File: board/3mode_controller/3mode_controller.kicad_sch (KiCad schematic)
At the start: 41 parts, among them IC1 DW01A, J1 Conn_01x04_Socket, J2 USB_C_Receptacle, Q1 FDN336P, SW1 reset, SW2 ChangeScreen, SW2 boot, SW4 SW_SPDT, U1 TP4056, U2 ESP32-S3-WROOM-1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

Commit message: first pcb version
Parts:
- removed R17 (x2): 5.1K, Resistor_SMD:R_0603_1608Metric_Pad0.98x0.95mm_HandSolder, symbol Device:R
- added H1, H2: MountingHole, MountingHole:MountingHole_3.2mm_M3_ISO14580_Pad, symbol Mechanical:MountingHole
- J1: footprint (none) -> Connector_PinHeader_2.54mm:PinHeader_1x04_P2.54mm_Vertical
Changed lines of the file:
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@@
   (junction (at 49.53 211.455) (diameter 0) (color 0 0 0 0)
   )
-  (junction (at 327.66 34.29) (diameter 0) (color 0 0 0 0)
-  )
   (junction (at 39.37 197.485) (diameter 0) (color 0 0 0 0)
   )
@@
   (junction (at 118.745 153.67) (diameter 0) (color 0 0 0 0)
   )
-  (junction (at 330.2 43.815) (diameter 0) (color 0 0 0 0)
-  )
   (junction (at 238.125 42.545) (diameter 0) (color 0 0 0 0)
   )
   (junction (at 41.275 45.085) (diameter 0) (color 0 0 0 0)
   )
-  (junction (at 325.12 54.61) (diameter 0) (color 0 0 0 0)
-  )
   (junction (at 215.265 56.515) (diameter 0) (color 0 0 0 0)
   )
@@
   )
   (junction (at 84.455 143.51) (diameter 0) (color 0 0 0 0)
-  )
-  (junction (at 325.12 45.72) (diameter 0) (color 0 0 0 0)
   )
   (junction (at 215.265 61.595) (diameter 0) (color 0 0 0 0)
@@
     (stroke (width 0) (type default))
   )
-  (wire (pts (xy 327.66 34.29) (xy 327.66 35.56))
-    (stroke (width 0) (type default))
-  )
   (wire (pts (xy 47.625 170.18) (xy 47.625 171.45))
     (stroke (width 0) (type default))
@@
     (stroke (width 0) (type default))
   )
-  (wire (pts (xy 330.2 52.705) (xy 330.2 54.61))
-    (stroke (width 0) (type default))
-  )
   (wire (pts (xy 39.37 233.045) (xy 49.53 233.045))
     (stroke (width 0) (type default))
@@
     (stroke (width 0) (type default))
   )
-  (wire (pts (xy 327.66 43.18) (xy 327.66 45.72))
-    (stroke (width 0) (type default))
-  )
   (wire (pts (xy 82.55 211.455) (xy 83.82 211.455))
     (stroke (width 0) (type default))
   )
-  (wire (pts (xy 327.66 45.72) (xy 325.12 45.72))
-    (stroke (width 0) (type default))
-  )
   (wire (pts (xy 327.66 33.655) (xy 327.66 34.29))
     (stroke (width 0) (type default))
@@
     (stroke (width 0) (type default))
   )
-  (wire (pts (xy 330.2 43.815) (xy 330.2 45.085))
-    (stroke (width 0) (type default))
-  )
   (wire (pts (xy 39.37 194.945) (xy 39.37 197.485))
     (stroke (width 0) (type default))
@@
     (stroke (width 0) (type default))
   )
-  (wire (pts (xy 325.12 33.655) (xy 325.12 45.72))
-    (stroke (width 0) (type default))
-  )
   (wire (pts (xy 215.265 61.595) (xy 215.265 62.865))
     (stroke (width 0) (type default))
@@
     (stroke (width 0) (type default))
   )
-  (wire (pts (xy 325.12 45.72) (xy 325.12 54.61))
-    (stroke (width 0) (type default))
-  )
   (wire (pts (xy 47.625 161.29) (xy 48.895 161.29))
     (stroke (width 0) (type default))
@@
     (stroke (width 0) (type default))
   )
-  (wire (pts (xy 325.12 54.61) (xy 325.12 55.245))
+  (wire (pts (xy 325.12 33.655) (xy 325.12 55.245))
     (stroke (width 0) (type default))
   )
@@
   )
   (wire (pts (xy 329.565 106.045) (xy 332.105 106.045))
-    (stroke (width 0) (type default))
-  )
-  (wire (pts (xy 330.2 54.61) (xy 325.12 54.61))
     (stroke (width 0) (type default))
   )
@@
     )
   )
+  (symbol (lib_id "Mechanical:MountingHole") (at 354.965 117.475 0) (unit 1)
+    (in_bom yes) (on_board yes) (dnp no)
+    (property "Reference" "H1" (at 358.14 116.2081 0)
+      (effects (font (size 1.27 1.27)) (justify left))
+    )
+    (property "Value" "MountingHole" (at 358.14 118.745 0)
+      (effects (font (size 1.27 1.27)) (justify left))
+    )
+    (property "Footprint" "MountingHole:MountingHole_3.2mm_M3_ISO14580_Pad" (at 354.965 117.475 0)
+      (effects (font (size 1.27 1.27)) hide)
+    )
+    (property "Datasheet" "~" (at 354.965 117.475 0)
+      (effects (font (size 1.27 1.27)) hide)
+    )
+    (instances
+      (project "bubblebutbot"
+        (path "/2cd1342d-9ef7-44f7-8a7d-ec49b5dc5750"
+          (reference "H1") (unit 1)
+        )
+      )
+      (project "3mode_controller"
+        (path "/64deb2d4-0f1e-4037-b447-7d4c34ae11e6"
+          (reference "H3") (unit 1)
+        )
+      )
+    )
+  )
   (symbol (lib_id "power:GND") (at 225.425 172.085 0) (unit 1)
     (in_bom yes) (on_board yes) (dnp no) (fields_autoplaced)
@@
       (effects (font (size 1.27 1.27)))
     )
-    (property "Footprint" "" (at 325.12 28.575 0)
+    (property "Footprint" "Connector_PinHeader_2.54mm:PinHeader_1x04_P2.54mm_Vertical" (at 325.12 28.575 0)
       (effects (font (size 1.27 1.27)) hide)
     )
@@
     )
   )
-  (symbol (lib_id "Device:R") (at 330.2 48.895 180) (unit 1)
-    (in_bom yes) (on_board yes) (dnp no)
-    (property "Reference" "R17" (at 331.978 47.6829 0)
-      (effects (font (size 1.27 1.27)) (justify right))
-    )
-    (property "Value" "5.1K" (at 331.978 50.1071 0)
-      (effects (font (size 1.27 1.27)) (justify right))
-    )
-    (property "Footprint" "Resistor_SMD:R_0603_1608Metric_Pad0.98x0.95mm_HandSolder" (at 331.978 48.895 90)
-      (effects (font (size 1.27 1.27)) hide)
-    )
-    (property "Datasheet" "https://www.lcsc.com/product-detail/Chip-Resistor-Surface-Mount_FOJAN-FRC0603J512-TS_C2907114.html" (at 330.2 48.895 0)
-      (effects (font (size 1.27 1.27)) hide)
-    )
-    (property "LCSC" "C2907114" (at 330.2 48.895 90)
-      (effects (font (size 1.27 1.27)) hide)
-    )
-    (pin "1")
-    (pin "2")
-    (instances
-      (project "bubblebutbot"
-        (path "/2cd1342d-9ef7-44f7-8a7d-ec49b5dc5750"
-          (reference "R17") (unit 1)
-        )
-      )
-      (project "3mode_controller"
-        (path "/64deb2d4-0f1e-4037-b447-7d4c34ae11e6"
-          (reference "R11") (unit 1)
-        )
-      )
-    )
-  )
   (symbol (lib_id "power:+5V") (at 238.125 42.545 0) (unit 1)
     (in_bom yes) (on_board yes) (dnp no) (fields_autoplaced)
@@
     )
   )
-  (symbol (lib_id "Device:R") (at 327.66 39.37 180) (unit 1)
-    (in_bom yes) (on_board yes) (dnp no)
-    (property "Reference" "R17" (at 330.835 38.2158 0)
-      (effects (font (size 1.27 1.27)) (justify right))
-    )
-    (property "Value" "5.1K" (at 330.835 40.64 0)
-      (effects (font (size 1.27 1.27)) (justify right))
-    )
-    (property "Footprint" "Resistor_SMD:R_0603_1608Metric_Pad0.98x0.95mm_HandSolder" (at 329.438 39.37 90)
-      (effects (font (size 1.27 1.27)) hide)
-    )
-    (property "Datasheet" "https://www.lcsc.com/product-detail/Chip-Resistor-Surface-Mount_FOJAN-FRC0603J512-TS_C2907114.html" (at 327.66 39.37 0)
-      (effects (font (size 1.27 1.27)) hide)
-    )
-    (property "LCSC" "C2907114" (at 327.66 39.37 90)
-      (effects (font (size 1.27 1.27)) hide)
-    )
-    (pin "1")
-    (pin "2")
-    (instances
-      (project "bubblebutbot"
-        (path "/2cd1342d-9ef7-44f7-8a7d-ec49b5dc5750"
-          (reference "R17") (unit 1)
-        )
-      )
-      (project "3mode_controller"
-        (path "/64deb2d4-0f1e-4037-b447-7d4c34ae11e6"
-          (reference "R8") (unit 1)
-        )
-      )
-    )
-  )
   (symbol (lib_id "power:GND") (at 80.645 170.18 0) (unit 1)
     (in_bom yes) (on_board yes) (dnp no) (fields_autoplaced)
@@
         )
       )
+    )
+  )
+  (symbol (lib_id "Mechanical:MountingHole") (at 354.965 123.19 0) (unit 1)
+    (in_bom yes) (on_board yes) (dnp no)
+    (property "Reference" "H2" (at 358.14 121.9231 0)
+      (effects (font (size 1.27 1.27)) (justify left))
+    )
+    (property "Value" "MountingHole" (at 358.14 124.46 0)
+      (effects (font (size 1.27 1.27)) (justify left))
+    )
+    (property "Footprint" "MountingHole:MountingHole_3.2mm_M3_ISO14580_Pad" (at 354.965 123.19 0)
+      (effects (font (size 1.27 1.27)) hide)
+    )
+    (property "Datasheet" "~" (at 354.965 123.19 0)
+      (effects (font (size 1.27 1.27)) hide)
+    )
+    (instances
+      (project "bubblebutbot"
+        (path "/2cd1342d-9ef7-44f7-8a7d-ec49b5dc5750"
+          (reference "H2") (unit 1)
+        )
+      )
+      (project "3mode_controller"
+        (path "/64deb2d4-0f1e-4037-b447-7d4c34ae11e6"
+          (reference "H4") (unit 1)
+        )
+      )

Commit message: updated one missing footprint
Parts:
- Q1: LCSC C475693 -> C19188376
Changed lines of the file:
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@@
       (effects (font (size 1.27 1.27) italic) (justify left) hide)
     )
-    (property "Datasheet" "https://datasheet.lcsc.com/lcsc/2001131004_Shikues-FDN336P_C475693.pdf" (at 111.125 151.13 0)
+    (property "Datasheet" "https://www.lcsc.com/product-detail/MOSFETs_Slkor-SLKORMICRO-Elec-FDN336P_C19188376.html" (at 111.125 151.13 0)
       (effects (font (size 1.27 1.27)) (justify left) hide)
     )
-    (property "LCSC" "C475693" (at 111.125 151.13 0)
+    (property "LCSC" "C19188376" (at 111.125 151.13 0)
       (effects (font (size 1.27 1.27)) hide)
     )

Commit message: first prototype board
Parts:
- removed C2: 10u, Capacitor_SMD:C_0603_1608Metric_Pad1.08x0.95mm_HandSolder, symbol Device:C
- removed H1, H2: MountingHole, MountingHole:MountingHole_3.2mm_M3_ISO14580_Pad, symbol Mechanical:MountingHole
- removed J1: Conn_01x04_Socket, Connector_PinHeader_2.54mm:PinHeader_1x04_P2.54mm_Vertical, symbol Connector:Conn_01x04_Socket
- removed SW2: ChangeScreen, Button_Switch_THT:SW_PUSH_6mm, symbol Switch:SW_Push
- removed U3: 18350-HOLDER, CustomFootprints:18350-Holder, symbol CustomSymbols:18350-HOLDER
- added J1: JST XH, Connector_JST:JST_PH_S2B-PH-K_1x02_P2.00mm_Horizontal, symbol Connector:Conn_01x02_Socket
- added SW3: SW_DIP_x04, Button_Switch_THT:SW_DIP_SPSTx04_Slide_9.78x12.34mm_W7.62mm_P2.54mm, symbol Switch:SW_DIP_x04
- U7, U8: LCSC C146170 -> C918854
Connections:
- net GND: now also U7.7 (SWa), U8.7 (SWa), SW3.5, SW3.6, SW3.7, SW3.8; no longer U7.9 (SWc), U8.9 (SWc)
- net VBAT+PROTECT: now also J1.1 (Pin_1)
- net JS_LEFT_IRQ: now reaches U7.8 (SWb)
- net JS_LEFT_IRQ: now also U2.22 (GPIO14/TOUCH14/ADC2_CH3/FSPIWP/FSPIDQS/SUBSPIWP)
- net at C4.2, IC1.6 (GND), U4.1 (S1): now also J1.2 (Pin_2)
- net JS_RIGHT_IRQ: now reaches U2.10 (GPIO17/U1TXD/ADC2_CH6)
- net JS_RIGHT_IRQ: now also U8.8 (SWb)
- net ESP32-PULLUP-1: now reaches U2.6 (GPIO6/TOUCH6/ADC1_CH5)
- net ESP32-PULLUP-1: now also SW3.4
- net ESP32-PULLUP-2: now reaches U2.7 (GPIO7/TOUCH7/ADC1_CH6)
- net ESP32-PULLUP-2: now also SW3.3
- net ESP32_BUTTON: no longer names the net of U2.5 (GPIO5/TOUCH5/ADC1_CH4)
- net ESP32_SCREEN_SCK renamed ESP32-PULLUP-3
- net ESP32-PULLUP-3: now also SW3.2
- net ESP32_SCREEN_SDA renamed ESP32-PULLUP-4
- net ESP32-PULLUP-4: now also SW3.1
- no-connect marks 47 -> 42
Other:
- note added: "Joystick RKJXV122400R Lever returns to center."
- note added: "swB = interrupt swA = grounded"
- note removed: "swd = interrupt swc = grounded"
- moved on the sheet: C13, R1, U2, U7, U8

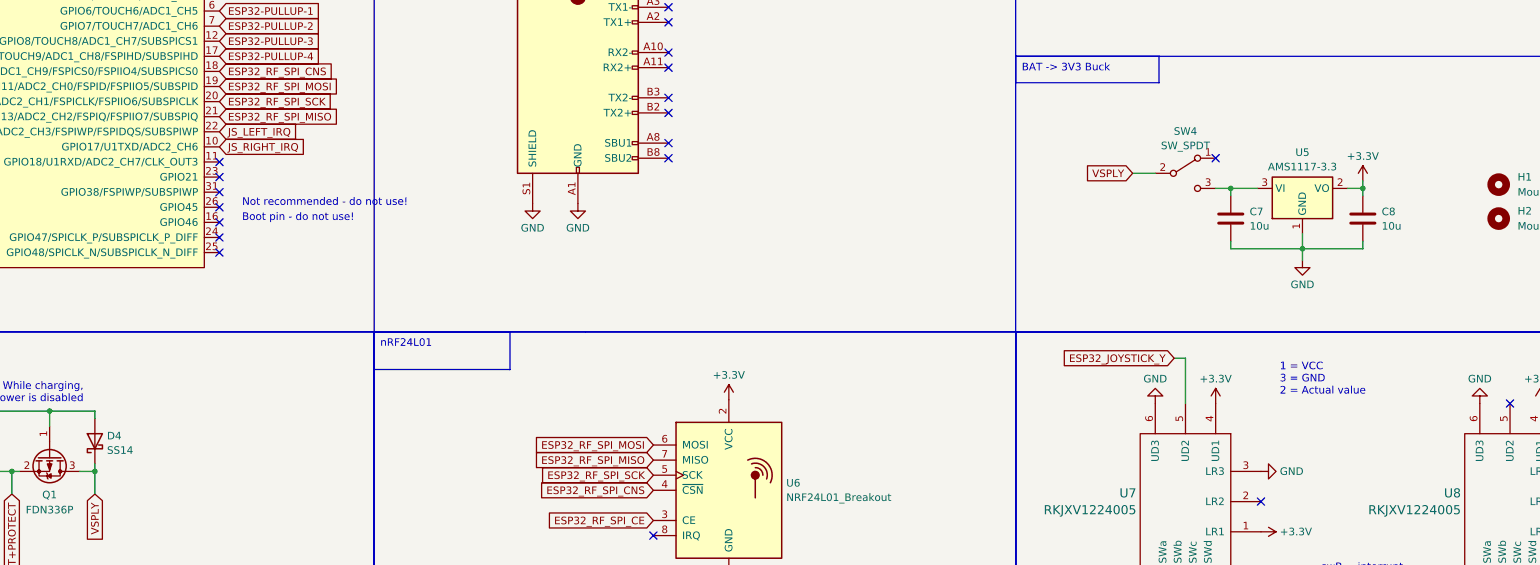
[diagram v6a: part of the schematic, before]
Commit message: v0.2.
Replaced diode and LDO
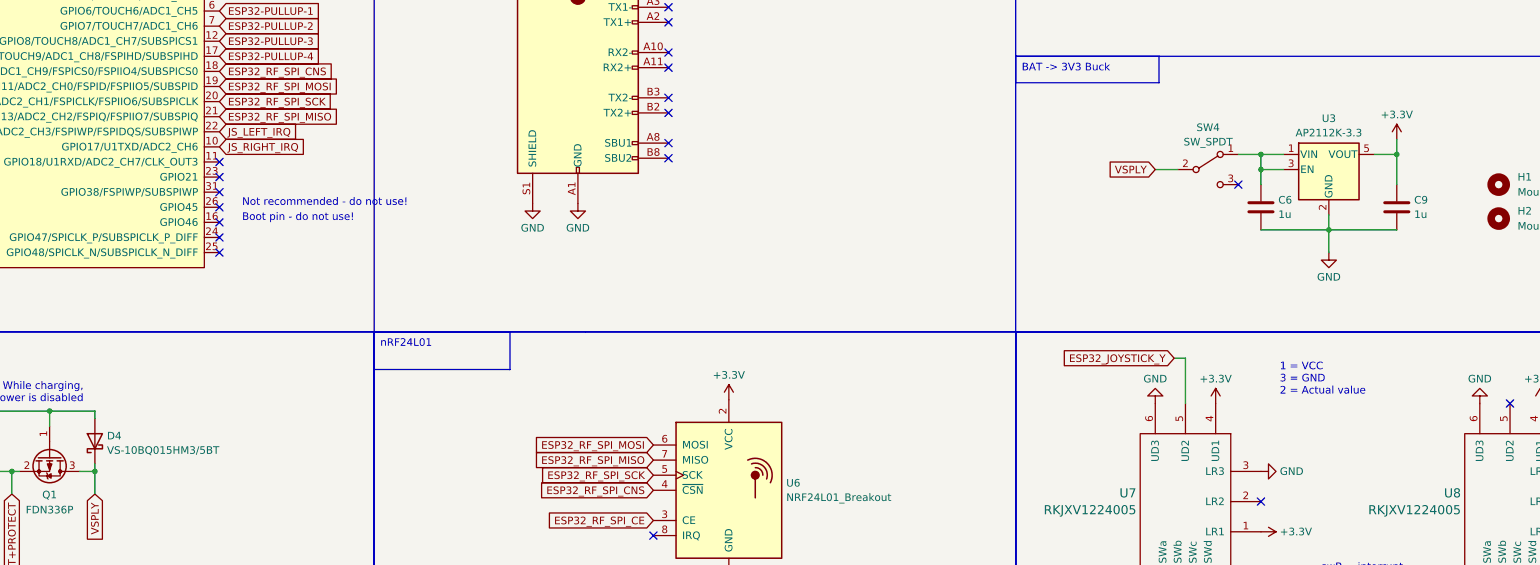
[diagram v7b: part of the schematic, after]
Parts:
- removed C7, C8: 10u, Capacitor_Tantalum_SMD:CP_EIA-3216-18_Kemet-A_Pad1.58x1.35mm_HandSolder, symbol Device:C
- removed U5: AMS1117-3.3, Package_TO_SOT_SMD:SOT-223-3_TabPin2, symbol Regulator_Linear:AMS1117-3.3
- added C6, C9: 1u, Capacitor_SMD:C_0603_1608Metric_Pad1.08x0.95mm_HandSolder, symbol Device:C
- added U3: AP2112K-3.3, Package_TO_SOT_SMD:SOT-23-5, symbol Regulator_Linear:AP2112K-3.3
- D4: value SS14 -> VS-10BQ015HM3/5BT; footprint Diode_SMD:D_SMA -> Diode_SMD:D_SMB; LCSC C2480 -> C413465
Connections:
- net +3.3V: now also C9.1, U3.5 (VOUT)
- net GND: now also C6.2, C9.2, U3.2 (GND)
- net at SW4.1 (A): now also C6.1, U3.1 (VIN), U3.3 (EN)
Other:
- moved on the sheet: SW4
